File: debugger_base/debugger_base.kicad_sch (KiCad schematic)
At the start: 59 parts, among them SW1 RST_FT, U1 74HC595, X1 USB_C_Receptacle_USB2.0_14P, X2 Channel A, X3 Channel B, X4 Channel C, X5 Channel D, Y1 12MHz

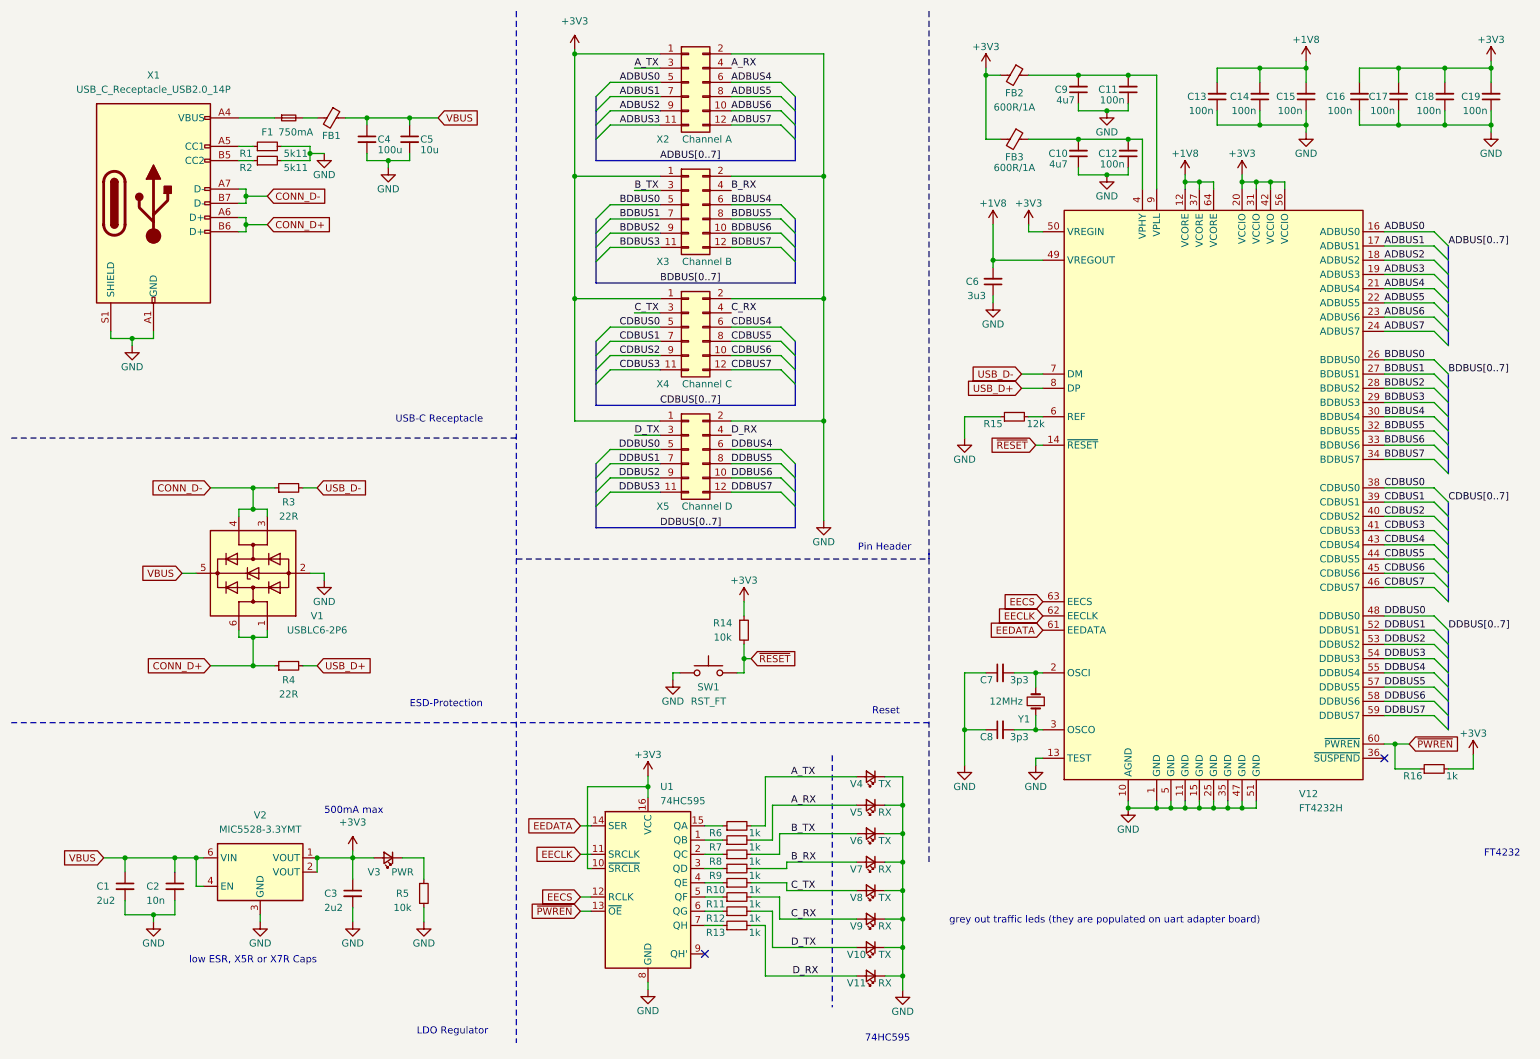
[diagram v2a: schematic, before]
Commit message: add led dip-switches; create pcb
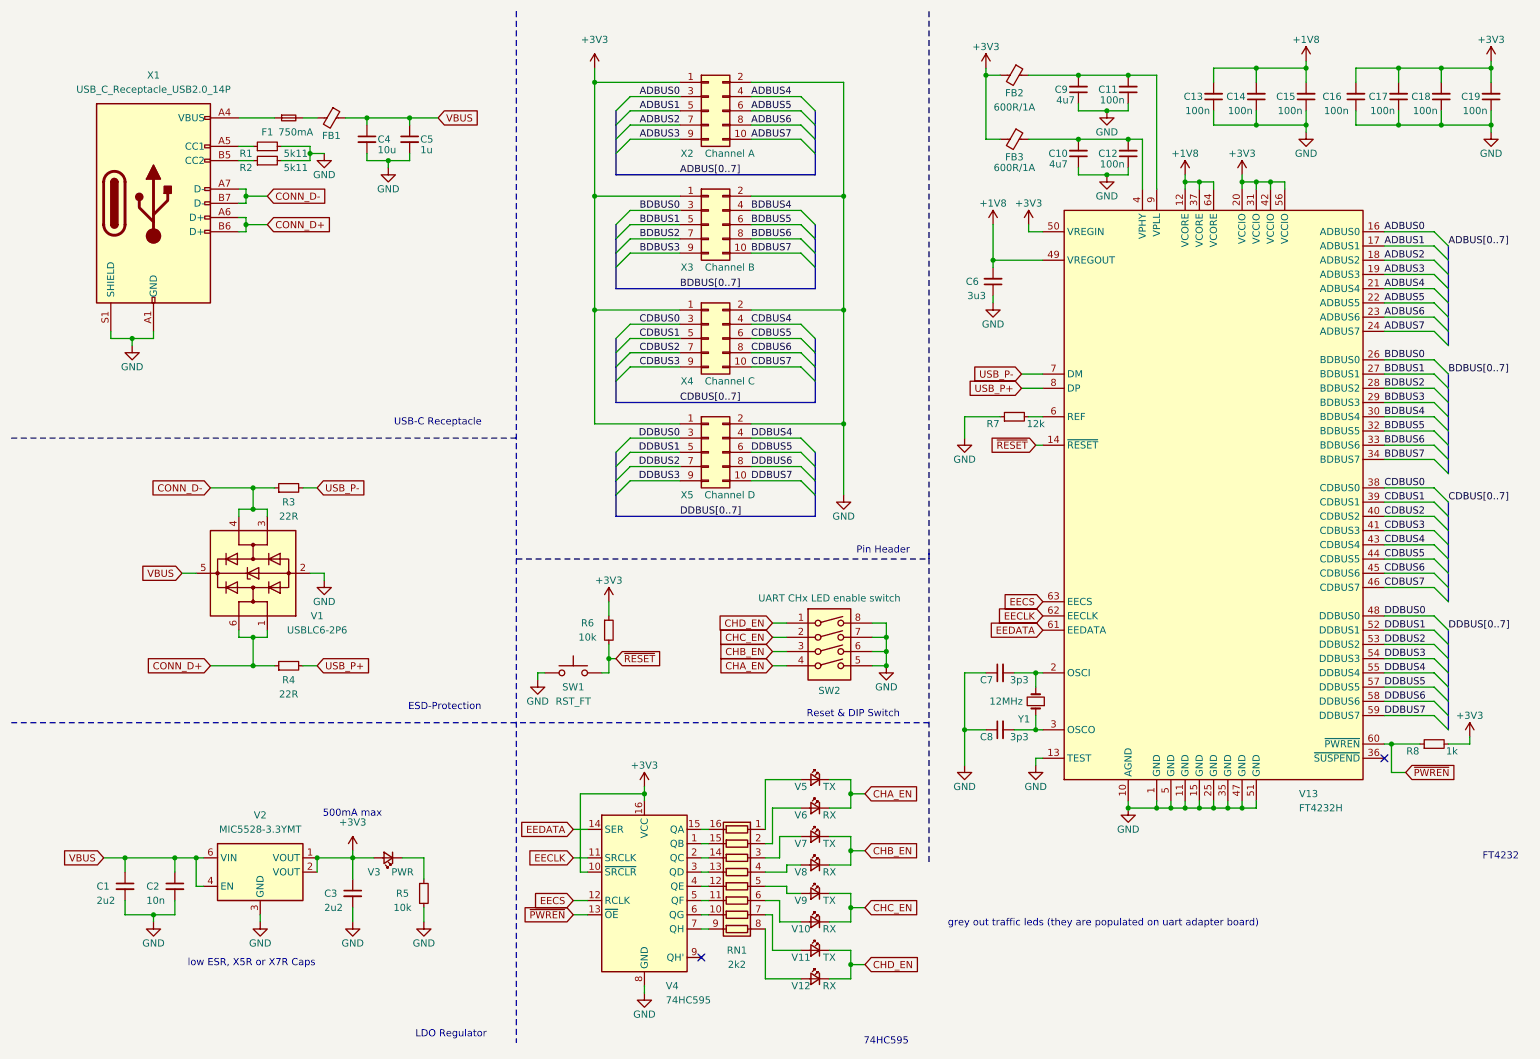
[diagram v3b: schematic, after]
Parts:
- removed R10, R11, R12, R13, R6, R7, R8, R9: 1k, Resistor_SMD:R_0402_1005Metric_Pad0.72x0.64mm_HandSolder, symbol Device:R_Small
- removed V4: TX, LED_SMD:LED_0603_1608Metric, symbol Device:LED_Small
- removed X2: Channel A, Connector_PinHeader_2.54mm:PinHeader_2x06_P2.54mm_Vertical_SMD, symbol Connector_Generic:Conn_02x06_Odd_Even
- removed X3: Channel B, Connector_PinHeader_2.54mm:PinHeader_2x06_P2.54mm_Vertical_SMD, symbol Connector_Generic:Conn_02x06_Odd_Even
- removed X4: Channel C, Connector_PinHeader_2.54mm:PinHeader_2x06_P2.54mm_Vertical_SMD, symbol Connector_Generic:Conn_02x06_Odd_Even
- removed X5: Channel D, Connector_PinHeader_2.54mm:PinHeader_2x06_P2.54mm_Vertical_SMD, symbol Connector_Generic:Conn_02x06_Odd_Even
- added RN1: 2k2, Resistor_SMD:R_Array_Convex_8x0602, symbol Device:R_Pack08
- added SW2: UART CHx LED enable switch, Button_Switch_SMD:SW_DIP_SPSTx04_Slide_6.7x11.72mm_W8.61mm_P2.54mm_LowProfile, symbol Switch:SW_DIP_x04
- added V12: RX, LED_SMD:LED_0603_1608Metric, symbol Device:LED_Small
- added X2: Channel A, Connector_PinHeader_2.54mm:PinHeader_2x05_P2.54mm_Vertical_SMD, symbol Connector_Generic:Conn_02x05_Odd_Even
- added X3: Channel B, Connector_PinHeader_2.54mm:PinHeader_2x05_P2.54mm_Vertical_SMD, symbol Connector_Generic:Conn_02x05_Odd_Even
- added X4: Channel C, Connector_PinHeader_2.54mm:PinHeader_2x05_P2.54mm_Vertical_SMD, symbol Connector_Generic:Conn_02x05_Odd_Even
- added X5: Channel D, Connector_PinHeader_2.54mm:PinHeader_2x05_P2.54mm_Vertical_SMD, symbol Connector_Generic:Conn_02x05_Odd_Even
- C4: value 100u -> 10u; footprint Capacitor_SMD:C_0805_2012Metric -> Capacitor_SMD:C_0402_1005Metric
- C5: value 10u -> 1u
- V10, V6, V8: value TX -> RX
- V11, V5, V7, V9: value RX -> TX
- V4: renamed from U1; footprint (none) -> Package_DFN_QFN:Texas_RUM0016A_WQFN-16-1EP_4x4mm_P0.65mm_EP2.6x2.6mm
- renumbered R14 to R6, R15 to R7, R16 to R8, V12 to V13
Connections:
- net +3V3: now also X2.1 (Pin_1), X3.1 (Pin_1), X4.1 (Pin_1), X5.1 (Pin_1)
- net ADBUS0: now also X2.3 (Pin_3)
- net ADBUS1: now also X2.5 (Pin_5)
- net ADBUS2: now also X2.7 (Pin_7)
- net ADBUS3: now also X2.9 (Pin_9)
- net ADBUS4: now also X2.4 (Pin_4)
- net ADBUS5: now also X2.6 (Pin_6)
- net ADBUS6: now also X2.8 (Pin_8)
- net ADBUS7: now also X2.10 (Pin_10)
- net BDBUS0: now also X3.3 (Pin_3)
- net BDBUS1: now also X3.5 (Pin_5)
- net BDBUS2: now also X3.7 (Pin_7)
- net BDBUS3: now also X3.9 (Pin_9)
- net BDBUS4: now also X3.4 (Pin_4)
- net BDBUS5: now also X3.6 (Pin_6)
- net BDBUS6: now also X3.8 (Pin_8)
- net BDBUS7: now also X3.10 (Pin_10)
- net CDBUS0: now also X4.3 (Pin_3)
- net CDBUS1: now also X4.5 (Pin_5)
- net CDBUS2: now also X4.7 (Pin_7)
- net CDBUS3: now also X4.9 (Pin_9)
- net CDBUS4: now also X4.4 (Pin_4)
- net CDBUS5: now also X4.6 (Pin_6)
- net CDBUS6: now also X4.8 (Pin_8)
- net CDBUS7: now also X4.10 (Pin_10)
- net DDBUS0: now also X5.3 (Pin_3)
- net DDBUS1: now also X5.5 (Pin_5)
- net DDBUS2: now also X5.7 (Pin_7)
- net DDBUS3: now also X5.9 (Pin_9)
- net DDBUS4: now also X5.4 (Pin_4)
- net DDBUS5: now also X5.6 (Pin_6)
- net DDBUS6: now also X5.8 (Pin_8)
- net DDBUS7: now also X5.10 (Pin_10)
- net GND: now also SW2.5, SW2.6, SW2.7, SW2.8, X2.2 (Pin_2), X3.2 (Pin_2), X4.2 (Pin_2), X5.2 (Pin_2); no longer V10.1 (K), V11.1 (K), V5.1 (K), V6.1 (K), V7.1 (K), V8.1 (K), V9.1 (K)
- net at V4.2 (QC): now also RN1.14 (R3.2)
- net at V4.1 (QB): now also RN1.15 (R2.2)
- net at V4.15 (QA): now also RN1.16 (R1.2)
- net at V4.3 (QD): now also RN1.13 (R4.2)
- net at V4.4 (QE): now also RN1.12 (R5.2)
- net at V4.5 (QF): now also RN1.11 (R6.2)
- net at V4.6 (QG): now also RN1.10 (R7.2)
- net at V4.7 (QH): now also RN1.9 (R8.2)
- net A_RX: no longer names the net of V5.2 (A)
- net A_RX: now also RN1.1 (R1.1)
- net B_RX: no longer names the net of V7.2 (A)
- net B_RX: now also RN1.3 (R3.1)
- net B_TX: no longer names the net of V6.2 (A)
- net B_TX: now also RN1.2 (R2.1)
- net C_RX: no longer names the net of V9.2 (A)
- net C_RX: now also RN1.5 (R5.1)
- net C_TX: no longer names the net of V8.2 (A)
- net C_TX: now also RN1.4 (R4.1)
- net D_RX: no longer names the net of V11.2 (A)
- net D_RX: now also RN1.7 (R7.1)
- net D_TX: no longer names the net of V10.2 (A)
- net D_TX: now also RN1.6 (R6.1)
- net USB_D+ renamed USB_P+
- net USB_D- renamed USB_P-
- new net: RN1.8 (R8.1), V12.2 (A)
- new net CHA_EN: SW2.4, V5.1 (K), V6.1 (K)
- new net CHB_EN: SW2.3, V7.1 (K), V8.1 (K)
- new net CHC_EN: SW2.2, V10.1 (K), V9.1 (K)
- new net CHD_EN: SW2.1, V11.1 (K), V12.1 (K)
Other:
- note added: "Reset & DIP Switch"
- note removed: "Reset"
- moved on the sheet: C13, C14, C16, C18, R6, R8, SW1, V4

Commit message: finish base board pcb
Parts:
- removed C1, C3: 2u2, Capacitor_SMD:C_0402_1005Metric_Pad0.74x0.62mm_HandSolder, symbol Device:C_Small
- removed C10, C9: 4u7, Capacitor_SMD:C_0402_1005Metric_Pad0.74x0.62mm_HandSolder, symbol Device:C_Small
- removed C11, C12, C13, C14, C15, C16, C17, C18, C19: 100n, Capacitor_SMD:C_0402_1005Metric_Pad0.74x0.62mm_HandSolder, symbol Device:C_Small
- removed C2: 10n, Capacitor_SMD:C_0402_1005Metric_Pad0.74x0.62mm_HandSolder, symbol Device:C_Small
- removed C4: 10u, Capacitor_SMD:C_0402_1005Metric, symbol Device:C_Small
- removed C5: 1u, Capacitor_SMD:C_0402_1005Metric, symbol Device:C_Small
- removed C6: 3u3, Capacitor_SMD:C_0402_1005Metric_Pad0.74x0.62mm_HandSolder, symbol Device:C_Small
- removed C7, C8: 3p3, Capacitor_SMD:C_0402_1005Metric_Pad0.74x0.62mm_HandSolder, symbol Device:C_Small
- removed F1: 750mA, Fuse:Fuse_0805_2012Metric, symbol Device:Fuse_Small
- removed FB1: FerriteBead_Small, Inductor_SMD:L_0603_1608Metric, symbol Device:FerriteBead_Small
- removed FB2, FB3: 600R/1A, Inductor_SMD:L_0603_1608Metric, symbol Device:FerriteBead_Small
- removed R1, R2: 5k11, Resistor_SMD:R_0402_1005Metric_Pad0.72x0.64mm_HandSolder, symbol Device:R_Small
- removed R3, R4: 22R, Resistor_SMD:R_0402_1005Metric_Pad0.72x0.64mm_HandSolder, symbol Device:R_Small
- removed R5, R6: 10k, Resistor_SMD:R_0402_1005Metric_Pad0.72x0.64mm_HandSolder, symbol Device:R_Small
- removed R7: 12k, Resistor_SMD:R_0402_1005Metric_Pad0.72x0.64mm_HandSolder, symbol Device:R_Small
- removed R8: 1k, Resistor_SMD:R_0402_1005Metric_Pad0.72x0.64mm_HandSolder, symbol Device:R_Small
- removed RN1: 2k2, Resistor_SMD:R_Array_Convex_8x0602, symbol Device:R_Pack08
- removed SW1: RST_FT, myLib:SW_SPST_EVQP2, symbol Switch:SW_Push
- removed SW2: UART CHx LED enable switch, Button_Switch_SMD:SW_DIP_SPSTx04_Slide_6.7x11.72mm_W8.61mm_P2.54mm_LowProfile, symbol Switch:SW_DIP_x04
- removed V1: USBLC6-2P6, Package_TO_SOT_SMD:SOT-666, symbol Power_Protection:USBLC6-2P6
- removed V10, V12, V6, V8: RX, LED_SMD:LED_0603_1608Metric, symbol Device:LED_Small
- removed V11, V5, V7, V9: TX, LED_SMD:LED_0603_1608Metric, symbol Device:LED_Small
- removed V13: FT4232H, Package_DFN_QFN:QFN-64-1EP_9x9mm_P0.5mm_EP4.35x4.35mm, symbol Interface_USB:FT4232H
- removed V2: MIC5528-3.3YMT, Package_TO_SOT_SMD:SOT-23-5, symbol Regulator_Linear:MIC5504-3.3YM5
- removed V3: PWR, LED_SMD:LED_0603_1608Metric, symbol Device:LED_Small
- removed V4: 74HC595, Package_DFN_QFN:Texas_RUM0016A_WQFN-16-1EP_4x4mm_P0.65mm_EP2.6x2.6mm, symbol 74xx:74HC595
- removed X1: USB_C_Receptacle_USB2.0_14P, Connector_USB:USB_C_Receptacle_G-Switch_GT-USB-7010ASV, symbol Connector:USB_C_Receptacle_USB2.0_14P
- removed X2: Channel A, Connector_PinHeader_2.54mm:PinHeader_2x05_P2.54mm_Vertical_SMD, symbol Connector_Generic:Conn_02x05_Odd_Even
- removed X3: Channel B, Connector_PinHeader_2.54mm:PinHeader_2x05_P2.54mm_Vertical_SMD, symbol Connector_Generic:Conn_02x05_Odd_Even
- removed X4: Channel C, Connector_PinHeader_2.54mm:PinHeader_2x05_P2.54mm_Vertical_SMD, symbol Connector_Generic:Conn_02x05_Odd_Even
- removed X5: Channel D, Connector_PinHeader_2.54mm:PinHeader_2x05_P2.54mm_Vertical_SMD, symbol Connector_Generic:Conn_02x05_Odd_Even
- removed Y1: 12MHz, Crystal:Crystal_SMD_3225-4Pin_3.2x2.5mm, symbol Device:Crystal_Small
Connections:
- no-connect marks 2 -> 0
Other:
- added sheet FT4232H (debugger_base_ft4232h.kicad_sch)
- added sheet LEDs, EEPROM (debugger_base_uart_leds.kicad_sch)
- added sheet Power (debugger_base_power.kicad_sch)
- note added: "check pinout (description, pin number, package) pullup on eeprom pins 74hc ldo oscillator load caps"
- note removed: "500mA max"
- note removed: "74HC595"
- note removed: "ESD-Protection"
- note removed: "FT4232"
- note removed: "LDO Regulator"
- note removed: "Pin Header"
- note removed: "Reset & DIP Switch"
- note removed: "USB-C Receptacle"
- note removed: "grey out traffic leds (they are populated on uart adapter board)"
- note removed: "low ESR, X5R or X7R Caps"

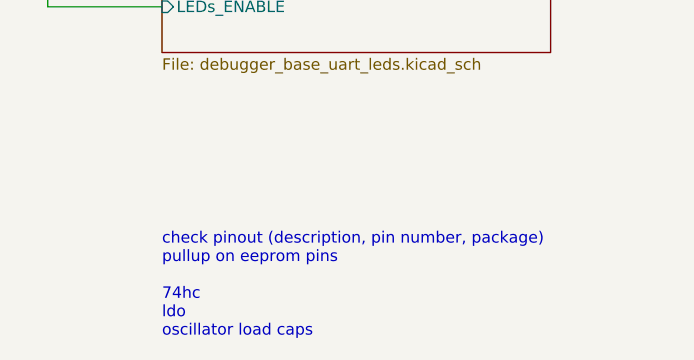
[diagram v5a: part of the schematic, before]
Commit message: decrease clearance of copper pours
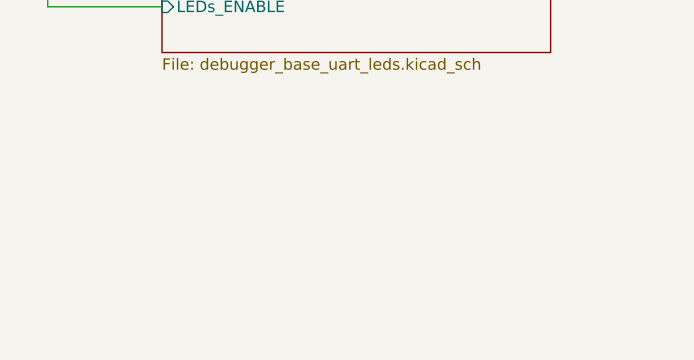
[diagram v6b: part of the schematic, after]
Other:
- note removed: "check pinout (description, pin number, package) pullup on eeprom pins 74hc ldo oscillator load caps"
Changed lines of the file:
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@@
 		(title "FT4232 Debugger Base")
 		(date "2024-02-10")
-		(rev "v0.1")
+		(rev "v1.0")
 		(comment 4 "Simon Brenninger")
 	)
@@
 		)
 	)
-	(text "check pinout (description, pin number, package)\npullup on eeprom pins\n\n74hc\nldo\noscillator load caps"
-		(exclude_from_sim no)
-		(at 177.8 180.34 0)
-		(effects
-			(font
-				(size 1.27 1.27)
-			)
-			(justify left bottom)
-		)
-	)
